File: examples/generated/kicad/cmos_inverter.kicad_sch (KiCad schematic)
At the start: 4 parts

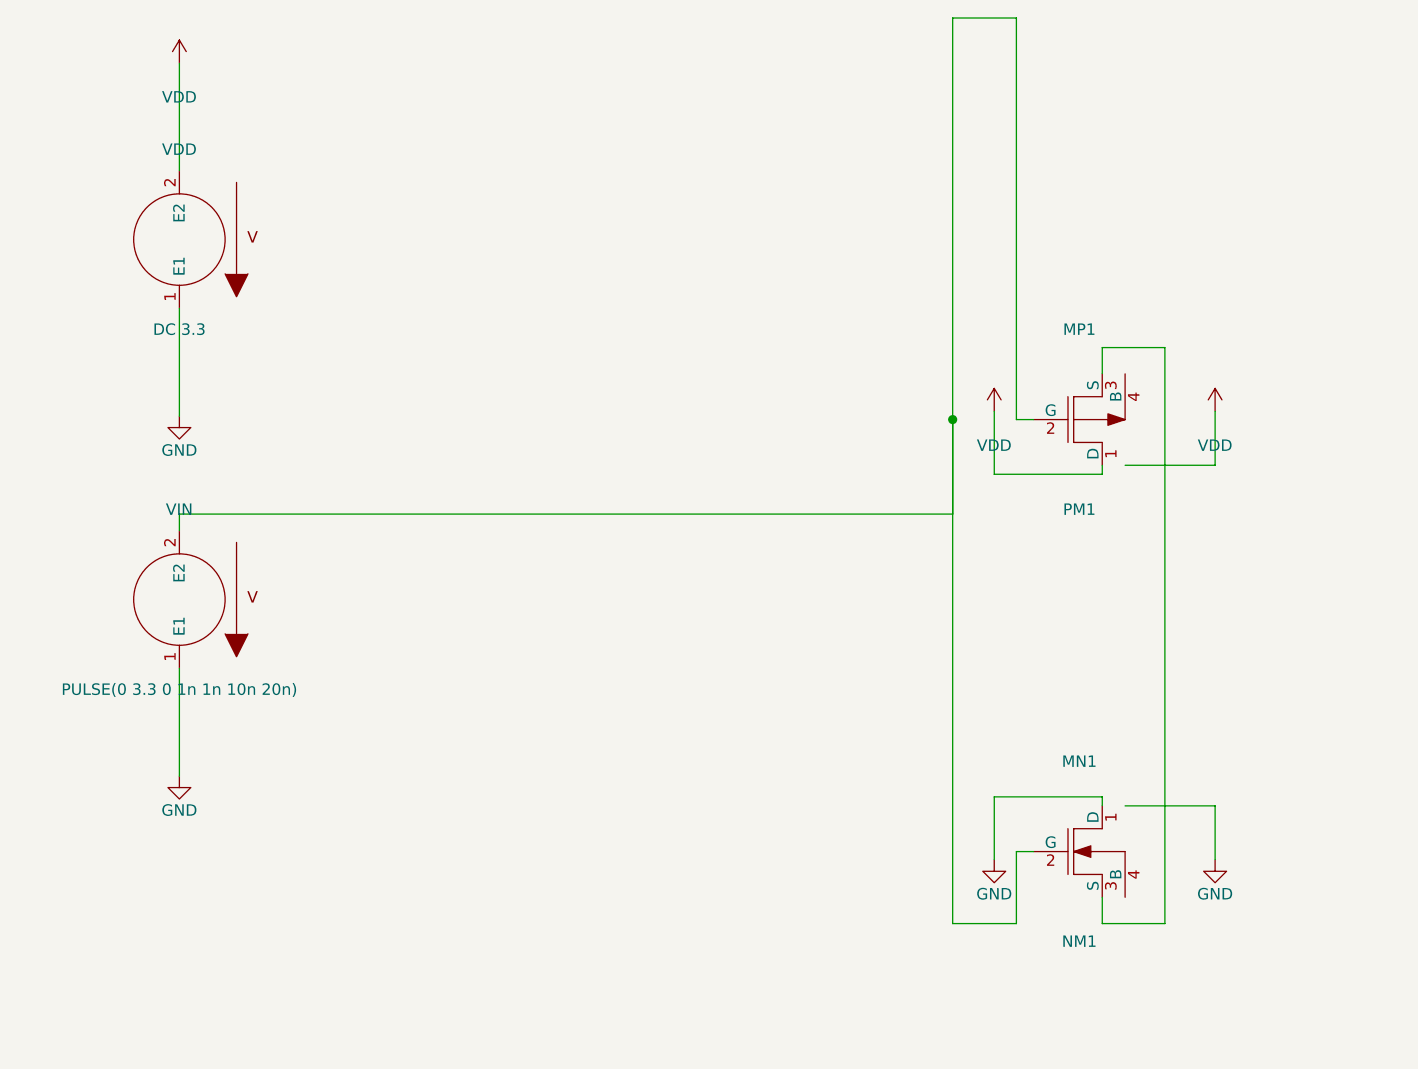
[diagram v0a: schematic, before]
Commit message: Ensure connectivity matches, as measured by opamp connectivity.
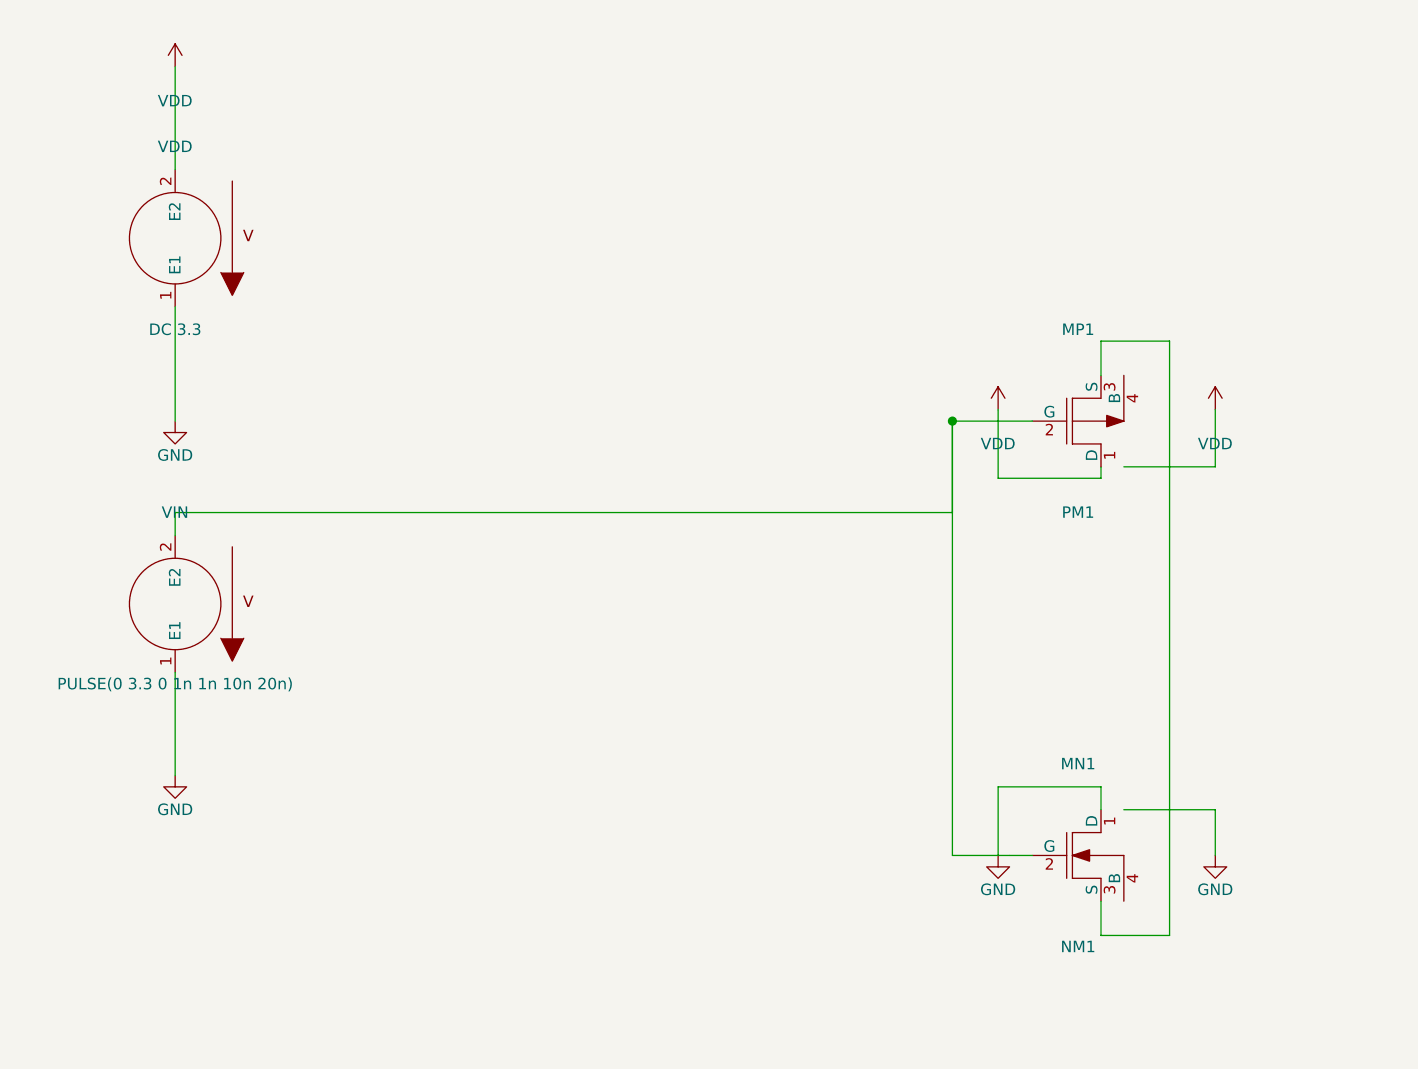
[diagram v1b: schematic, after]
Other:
- moved on the sheet: VIN

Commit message: Refactor further.
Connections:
- net vin: now reaches MN1.2 (G), MP1.2 (G), VIN.2 (E2)
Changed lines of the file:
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@@
     )
+  )
+  (label "vin" (at 135.89 90.17 0)
+    (effects (font (size 1.27 1.27)))
+  )
+  (label "vout" (at 152.40 114.30 0)
+    (effects (font (size 1.27 1.27)))
   )
   (wire (pts (xy 49.53 62.23) (xy 49.53 50.80))

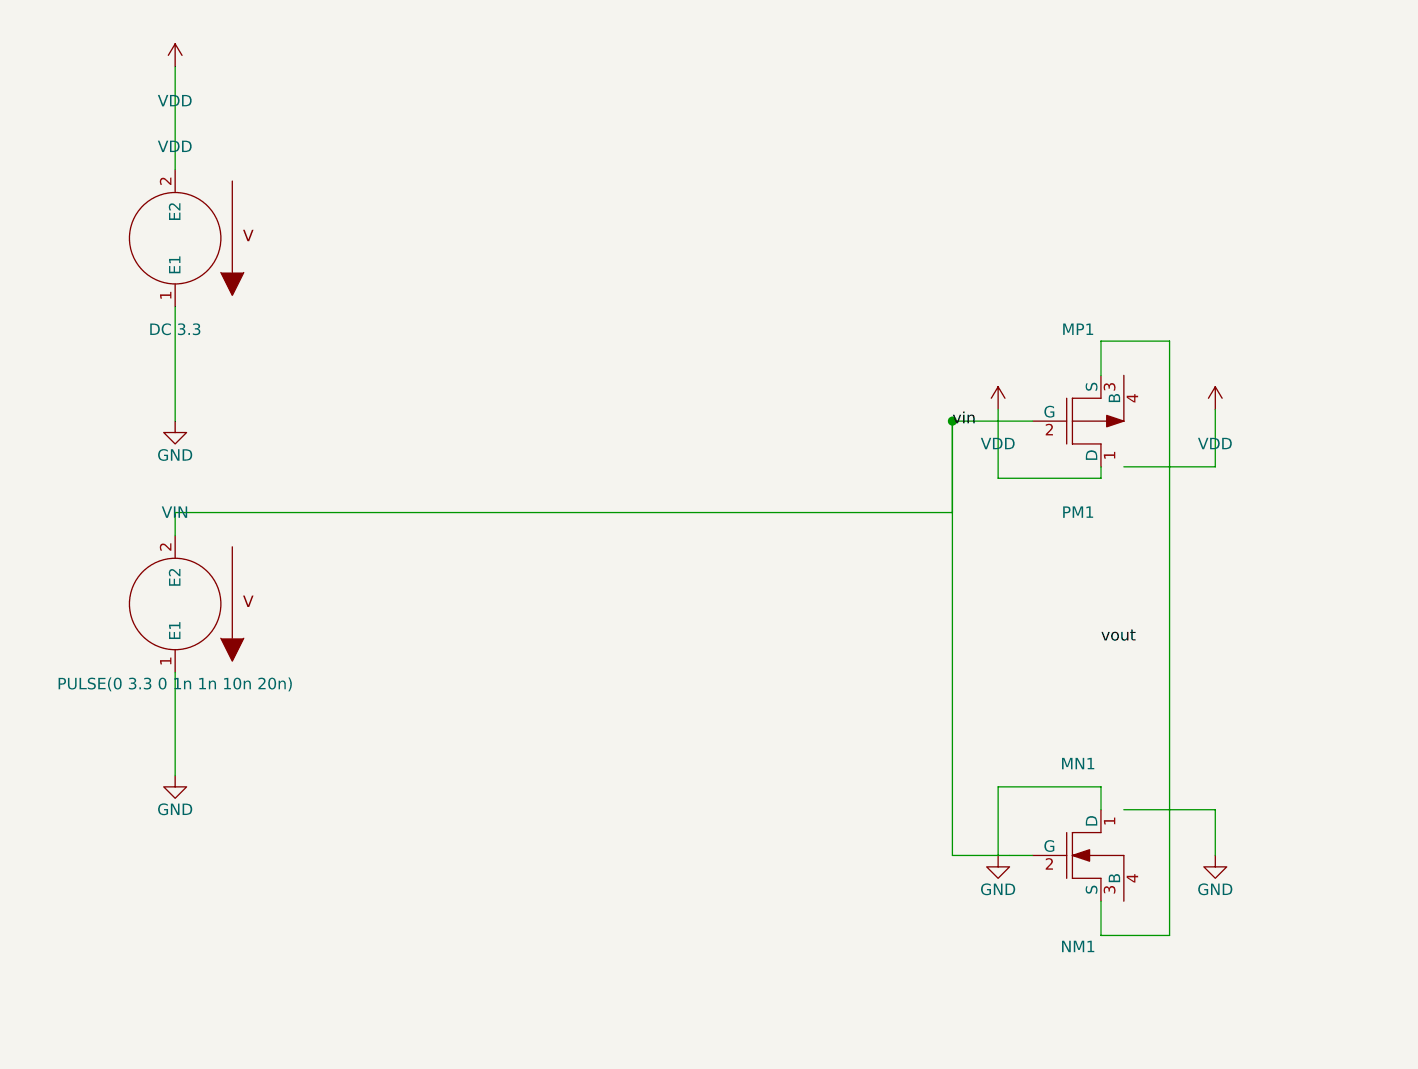
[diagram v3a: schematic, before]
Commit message: Attempt to fix CMOS schematic layout.
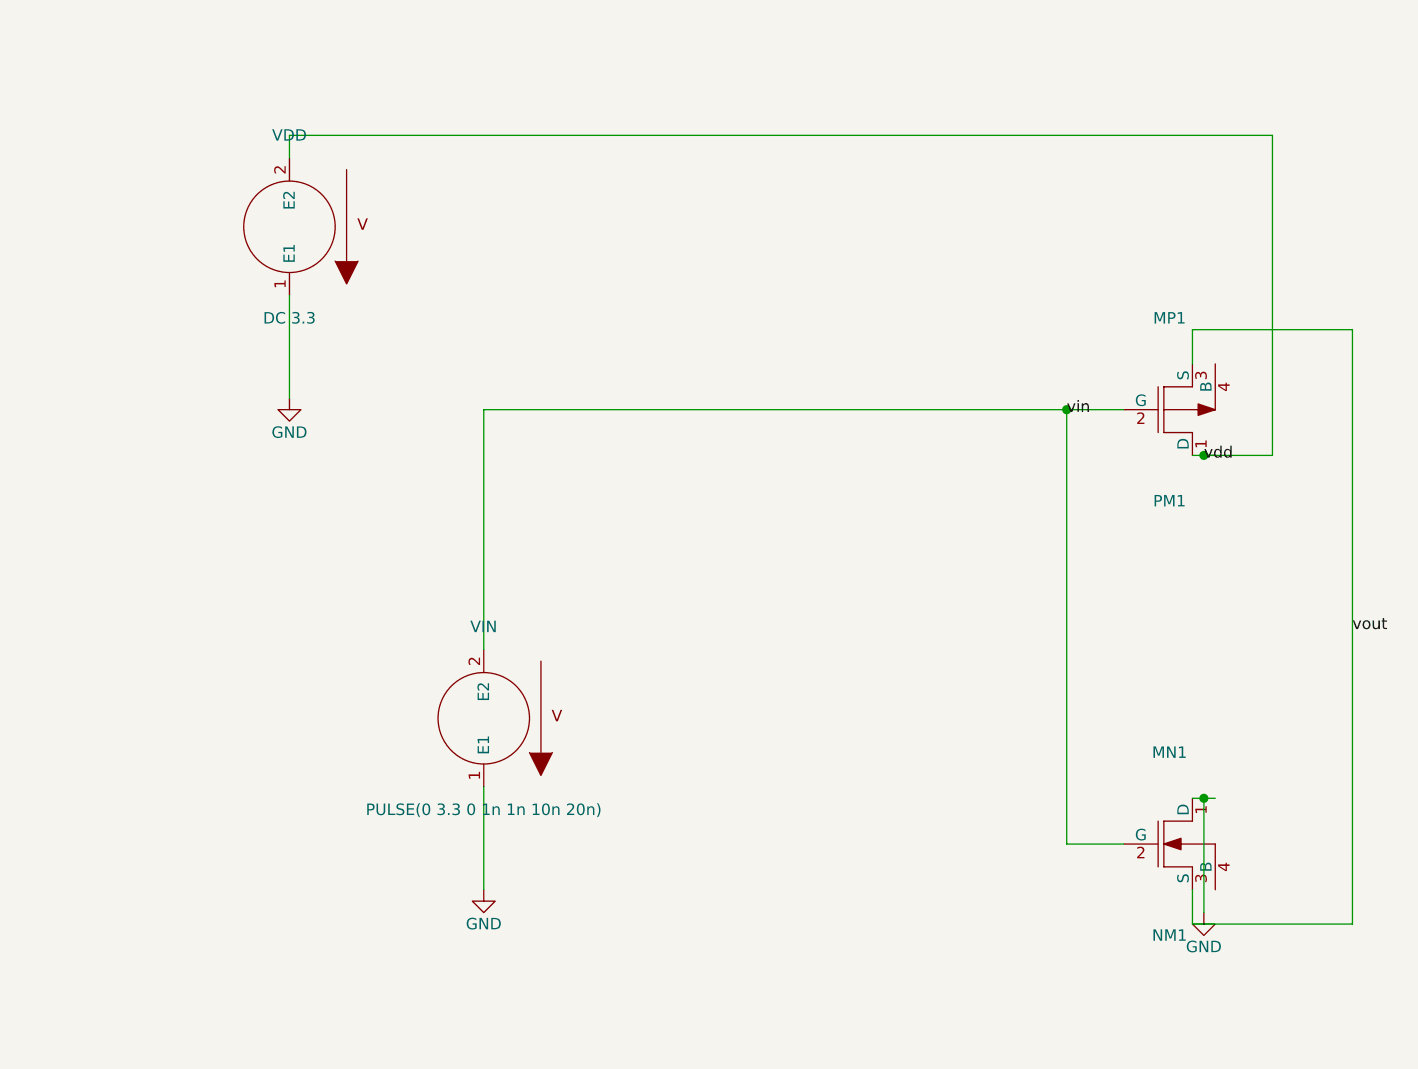
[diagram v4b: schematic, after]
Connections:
- net vout: now also MN1.3 (S), MP1.3 (S)
- net VDD renamed vdd
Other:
- moved on the sheet: MN1, MP1, VDD, VIN

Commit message: Attempt to fix routing issues.
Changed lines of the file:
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@@
     )
   )
-  (label "vin" (at 148.59 88.90 0)
+  (label "vin" (at 148.59 115.57 0)
     (effects (font (size 1.27 1.27)))
   )
@@
     (effects (font (size 1.27 1.27)))
   )
-  (label "vout" (at 180.34 113.03 0)
+  (label "vout" (at 162.56 113.03 0)
     (effects (font (size 1.27 1.27)))
   )
@@
     (stroke (width 0) (type solid) (color 0 0 0 0))
   )
-  (wire (pts (xy 83.82 115.57) (xy 83.82 88.90))
+  (wire (pts (xy 148.59 88.90) (xy 148.59 137.16))
     (stroke (width 0) (type solid) (color 0 0 0 0))
   )
-  (wire (pts (xy 83.82 88.90) (xy 148.59 88.90))
+  (wire (pts (xy 83.82 115.57) (xy 148.59 115.57))
     (stroke (width 0) (type solid) (color 0 0 0 0))
   )
@@
   )
   (wire (pts (xy 154.94 137.16) (xy 148.59 137.16))
-    (stroke (width 0) (type solid) (color 0 0 0 0))
-  )
-  (wire (pts (xy 148.59 137.16) (xy 148.59 88.90))
     (stroke (width 0) (type solid) (color 0 0 0 0))
   )
@@
     (stroke (width 0) (type solid) (color 0 0 0 0))
   )
-  (wire (pts (xy 162.56 83.82) (xy 162.56 80.01))
-    (stroke (width 0) (type solid) (color 0 0 0 0))
-  )
-  (wire (pts (xy 162.56 80.01) (xy 180.34 80.01))
-    (stroke (width 0) (type solid) (color 0 0 0 0))
-  )
-  (wire (pts (xy 180.34 80.01) (xy 180.34 113.03))
-    (stroke (width 0) (type solid) (color 0 0 0 0))
-  )
-  (wire (pts (xy 162.56 142.24) (xy 162.56 146.05))
-    (stroke (width 0) (type solid) (color 0 0 0 0))
-  )
-  (wire (pts (xy 162.56 146.05) (xy 180.34 146.05))
-    (stroke (width 0) (type solid) (color 0 0 0 0))
-  )
-  (wire (pts (xy 180.34 146.05) (xy 180.34 113.03))
+  (wire (pts (xy 162.56 83.82) (xy 162.56 142.24))
     (stroke (width 0) (type solid) (color 0 0 0 0))
   )
@@
     (stroke (width 0) (type solid) (color 0 0 0 0))
   )
-  (junction (at 148.59 88.90) (diameter 1.016) (color 0 0 0 0))
+  (junction (at 148.59 115.57) (diameter 1.016) (color 0 0 0 0))
   (junction (at 163.83 93.98) (diameter 1.016) (color 0 0 0 0))
   (junction (at 163.83 132.08) (diameter 1.016) (color 0 0 0 0))

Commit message: Attempt again to fix cmos topology.
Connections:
- net GND: now also MN1.3 (S), MN1.4 (B); no longer MN1.1 (D)
- net vdd: now also MP1.3 (S), MP1.4 (B); no longer MP1.1 (D)
- net vout: now also MN1.1 (D), MP1.1 (D); no longer MN1.3 (S), MP1.3 (S)
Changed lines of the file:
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@@
     )
   )
-  (symbol (lib_id "GND") (at 163.83 144.78 0) (unit 1)
+  (symbol (lib_id "GND") (at 163.83 154.94 0) (unit 1)
     (in_bom yes) (on_board yes)
-    (property "Reference" "#PWR0003" (at 163.83 140.97 0)
+    (property "Reference" "#PWR0003" (at 163.83 151.13 0)
       (effects (font (size 1.27 1.27)) hide)
     )
-    (property "Value" "GND" (at 163.83 148.59 0)
+    (property "Value" "GND" (at 163.83 158.75 0)
       (effects (font (size 1.27 1.27)))
     )
@@
     )
   )
-  (label "vin" (at 148.59 115.57 0)
+  (label "vin" (at 144.78 115.57 0)
     (effects (font (size 1.27 1.27)))
   )
-  (label "vdd" (at 163.83 93.98 0)
+  (label "vdd" (at 163.83 83.82 0)
     (effects (font (size 1.27 1.27)))
   )
@@
     (stroke (width 0) (type solid) (color 0 0 0 0))
   )
-  (wire (pts (xy 148.59 88.90) (xy 148.59 137.16))
+  (wire (pts (xy 144.78 88.90) (xy 144.78 137.16))
     (stroke (width 0) (type solid) (color 0 0 0 0))
   )
-  (wire (pts (xy 83.82 115.57) (xy 148.59 115.57))
+  (wire (pts (xy 83.82 115.57) (xy 144.78 115.57))
     (stroke (width 0) (type solid) (color 0 0 0 0))
   )
-  (wire (pts (xy 154.94 88.90) (xy 148.59 88.90))
+  (wire (pts (xy 154.94 88.90) (xy 144.78 88.90))
     (stroke (width 0) (type solid) (color 0 0 0 0))
   )
-  (wire (pts (xy 154.94 137.16) (xy 148.59 137.16))
+  (wire (pts (xy 154.94 137.16) (xy 144.78 137.16))
     (stroke (width 0) (type solid) (color 0 0 0 0))
   )
@@
     (stroke (width 0) (type solid) (color 0 0 0 0))
   )
-  (wire (pts (xy 62.23 58.42) (xy 171.45 58.42))
+  (wire (pts (xy 62.23 58.42) (xy 163.83 58.42))
     (stroke (width 0) (type solid) (color 0 0 0 0))
   )
-  (wire (pts (xy 171.45 58.42) (xy 171.45 93.98))
+  (wire (pts (xy 163.83 58.42) (xy 163.83 83.82))
     (stroke (width 0) (type solid) (color 0 0 0 0))
   )
-  (wire (pts (xy 171.45 93.98) (xy 163.83 93.98))
+  (wire (pts (xy 162.56 83.82) (xy 163.83 83.82))
     (stroke (width 0) (type solid) (color 0 0 0 0))
   )
-  (wire (pts (xy 162.56 93.98) (xy 163.83 93.98))
+  (wire (pts (xy 165.10 83.82) (xy 163.83 83.82))
     (stroke (width 0) (type solid) (color 0 0 0 0))
   )
-  (wire (pts (xy 165.10 93.98) (xy 163.83 93.98))
+  (wire (pts (xy 162.56 93.98) (xy 162.56 132.08))
     (stroke (width 0) (type solid) (color 0 0 0 0))
   )
-  (wire (pts (xy 162.56 83.82) (xy 162.56 142.24))
+  (wire (pts (xy 162.56 142.24) (xy 163.83 142.24))
     (stroke (width 0) (type solid) (color 0 0 0 0))
   )
-  (wire (pts (xy 162.56 132.08) (xy 163.83 132.08))
+  (wire (pts (xy 165.10 142.24) (xy 163.83 142.24))
     (stroke (width 0) (type solid) (color 0 0 0 0))
   )
-  (wire (pts (xy 165.10 132.08) (xy 163.83 132.08))
+  (wire (pts (xy 163.83 154.94) (xy 163.83 147.32))
     (stroke (width 0) (type solid) (color 0 0 0 0))
   )
-  (wire (pts (xy 163.83 144.78) (xy 163.83 132.08))
+  (wire (pts (xy 163.83 147.32) (xy 171.45 147.32))
     (stroke (width 0) (type solid) (color 0 0 0 0))
   )
-  (junction (at 148.59 115.57) (diameter 1.016) (color 0 0 0 0))
-  (junction (at 163.83 93.98) (diameter 1.016) (color 0 0 0 0))
-  (junction (at 163.83 132.08) (diameter 1.016) (color 0 0 0 0))
+  (wire (pts (xy 171.45 147.32) (xy 171.45 142.24))
+    (stroke (width 0) (type solid) (color 0 0 0 0))
+  )
+  (wire (pts (xy 171.45 142.24) (xy 163.83 142.24))
+    (stroke (width 0) (type solid) (color 0 0 0 0))
+  )
+  (junction (at 144.78 115.57) (diameter 1.016) (color 0 0 0 0))
+  (junction (at 163.83 83.82) (diameter 1.016) (color 0 0 0 0))
+  (junction (at 163.83 142.24) (diameter 1.016) (color 0 0 0 0))
   (sheet_instances
     (path "/" (page "1"))
